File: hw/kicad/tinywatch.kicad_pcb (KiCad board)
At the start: 2 copper layers, 24.9 x 23.1 mm, 18 parts, among them J1 Conn_01x04, J2 Conn_01x30, SW1 SW_Push, SW2 SW_Push, SW3 SW_Push, U1 ATtiny1614-SS

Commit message: R2 hardware
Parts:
- removed R1: 4k7, Resistor_SMD:R_0603_1608Metric_Pad0.98x0.95mm_HandSolder
- added C10: 8.2p, Capacitor_SMD:C_0603_1608Metric_Pad1.08x0.95mm_HandSolder, F.Cu at (166.9, 87.5)
- added C9: 8.2p, Capacitor_SMD:C_0603_1608Metric_Pad1.08x0.95mm_HandSolder, F.Cu at (166.9, 84.2)
- added J3: Conn_01x01_Pin, Connector_Wire:SolderWire-0.25sqmm_1x01_D0.65mm_OD1.7mm, F.Cu at (148.2, 99.9)
- added J4: Conn_01x01_Pin, Connector_Wire:SolderWire-0.25sqmm_1x01_D0.65mm_OD1.7mm, F.Cu at (159.5, 99.9)
- added Y1: 32.768 kHz, Crystal:Crystal_DS10_D1.0mm_L4.3mm_Horizontal, F.Cu at (164.1, 88.8)
- moved U1 4.56 mm to (161.5, 82.3)
- moved C2 3.84 mm to (165.9, 87.4)
- moved C3 3.84 mm to (162.1, 87.4)
- moved C5 3.13 mm to (155.3, 84.8)
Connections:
- J1 pad 1: Net-(J1-Pad1) -> Net-(J1-Pin_1)
- J1 pad 2: Net-(J1-Pad2) -> Net-(J1-Pin_2)
- J1 pad 3: Net-(J1-Pad3) -> Net-(J1-Pin_3)
- U1 pad 10: Net-(R1-Pad2) -> Net-(J1-Pin_3)
- U1 pad 11: VCCQ -> Net-(J1-Pin_2)
- U1 pad 12: unconnected-(U1-Pad12) -> Net-(J1-Pin_1)
- U1 pad 2: unconnected-(U1-Pad2) -> VCCQ
- U1 pad 6: Net-(J1-Pad1) -> Net-(U1-PB3)
- U1 pad 7: Net-(J1-Pad2) -> Net-(U1-PB2)
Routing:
- net GND: track 65.0 -> 0.00 mm, vias 1 -> 2
- net Net-(J1-Pad1): track 31.3 -> 0.00 mm
- net Net-(J1-Pad2): track 24.8 -> 0.00 mm
- net Net-(J1-Pin_3): track 0.00 -> 14.4 mm
- net Net-(J1-Pin_2): track 0.00 -> 12.3 mm
- net Net-(J1-Pin_1): track 0.00 -> 10.8 mm
- net VCC: track 29.2 -> 20.0 mm
- net Net-(R1-Pad2): track 9.00 -> 0.00 mm
- net Net-(U1-PB3): track 0.00 -> 7.94 mm
- net Net-(U1-PB2): track 0.00 -> 7.78 mm
- net Net-(U1-PA7): track 6.33 -> 12.2 mm
- net Net-(J2-Pin_18): track 14.2 -> 19.3 mm
- net Net-(U1-PA6): track 5.20 -> 10.0 mm
- net Net-(U1-PA5): track 13.1 -> 17.2 mm
- net Net-(J2-Pin_3): track 6.74 -> 3.38 mm
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
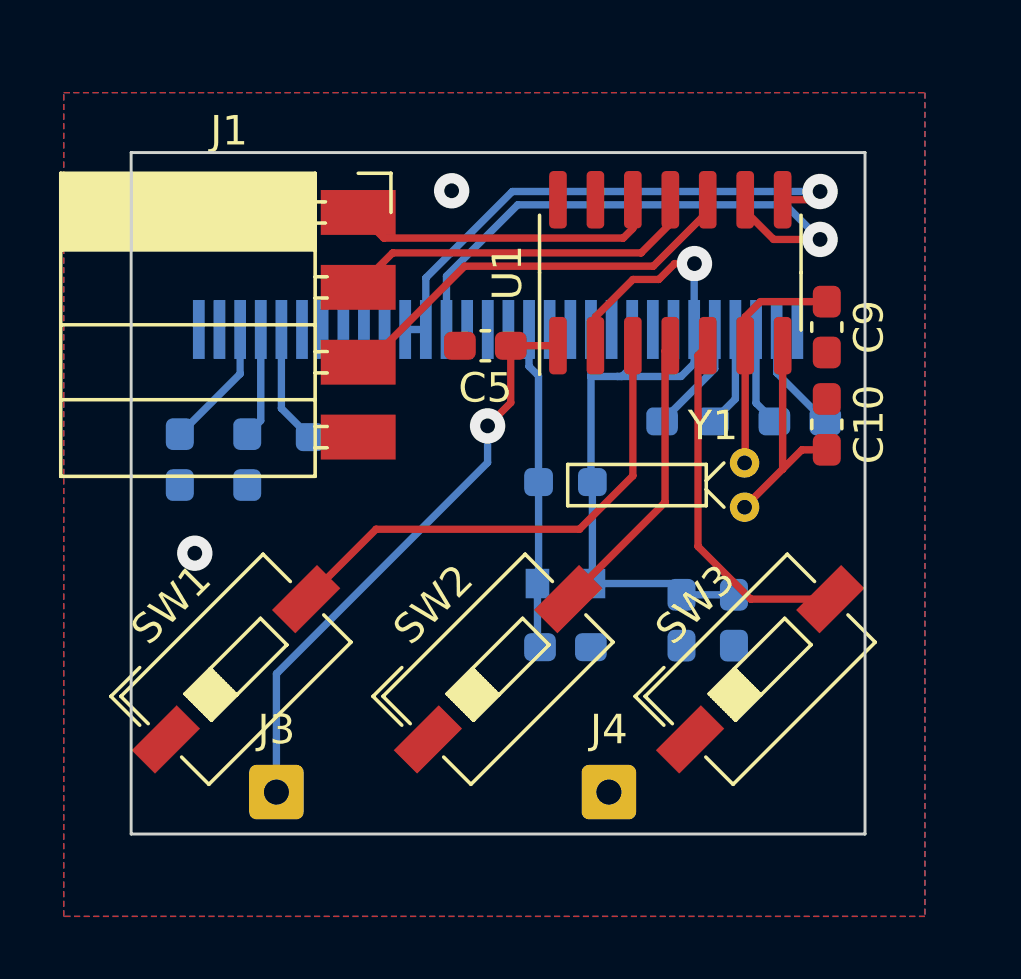
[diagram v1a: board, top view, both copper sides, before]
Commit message: Updated BOM and README
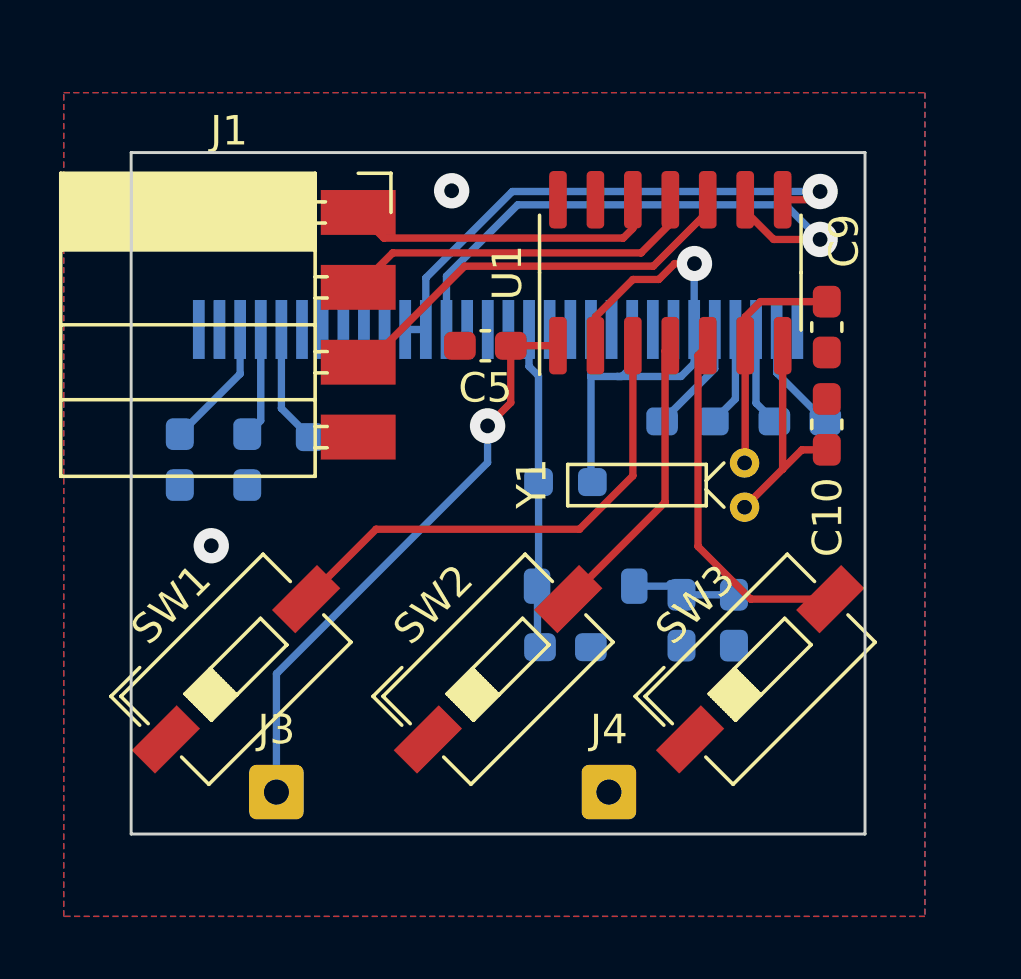
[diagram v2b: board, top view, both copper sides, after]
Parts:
- D1: footprint Diode_SMD:D_SOD-110 -> Diode_SMD:D_SOD-123
- moved D1 0.69 mm to (158.7, 92.9)
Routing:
- net VCCQ: track 27.6 -> 23.3 mm

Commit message: Left a trace disconnected, whoops
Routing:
- net VCCQ: track 23.3 -> 27.4 mm

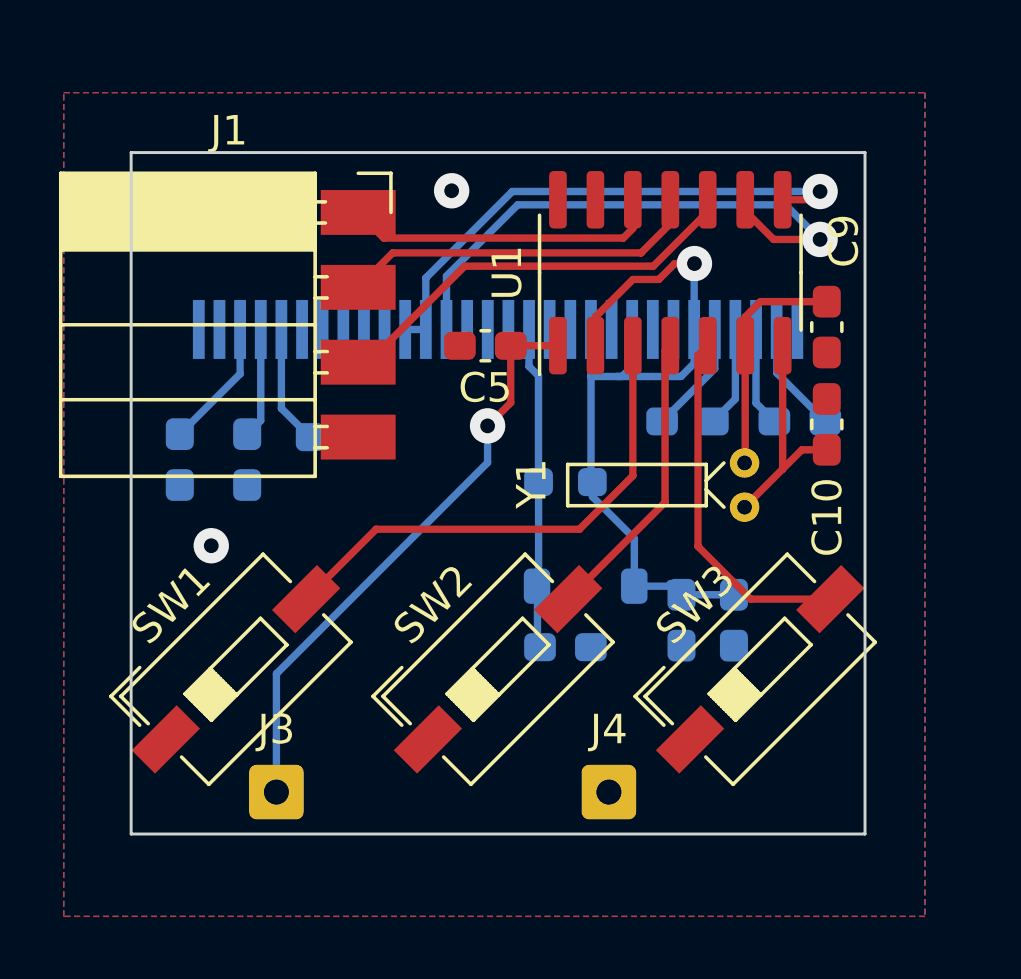
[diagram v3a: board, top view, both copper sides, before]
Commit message: Replaced the crystal with a more precise TXCO
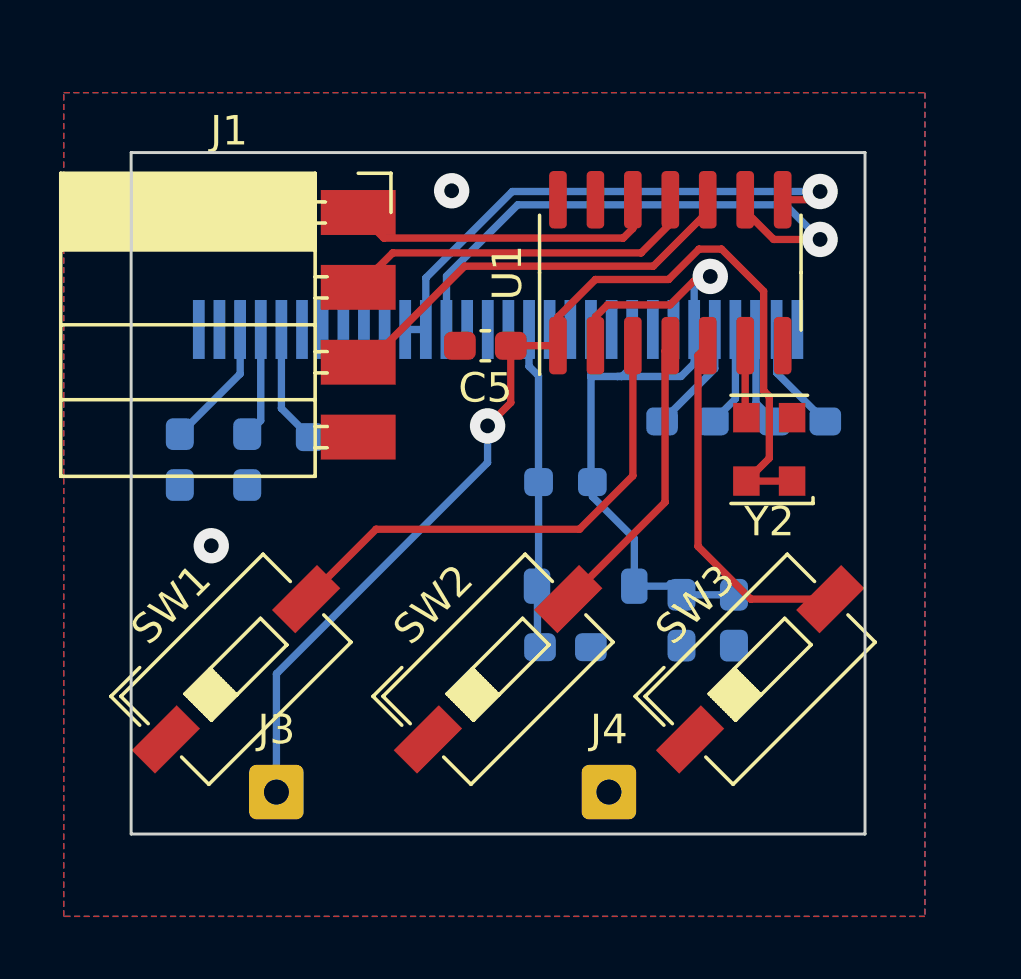
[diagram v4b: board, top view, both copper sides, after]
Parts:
- removed C10, C9: 8.2p, Capacitor_SMD:C_0603_1608Metric_Pad1.08x0.95mm_HandSolder
- removed Y1: 32.768 kHz, Crystal:Crystal_DS10_D1.0mm_L4.3mm_Horizontal
- added Y2: ECS-327TXO-30, Oscillator:Oscillator_SMD_EuroQuartz_XO32-4Pin_3.2x2.5mm, F.Cu at (164.9, 88.3)
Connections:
- U1 pad 7: Net-(U1-PB2) -> unconnected-(U1-PB2-Pad7)
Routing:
- net VCC: track 20.0 -> 37.9 mm
- net Net-(U1-PB2): track 7.78 -> 0.00 mm
- net Net-(U1-PB3): track 7.94 -> 2.46 mm

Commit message: Replaced TXCO footprint with a more solderable variant
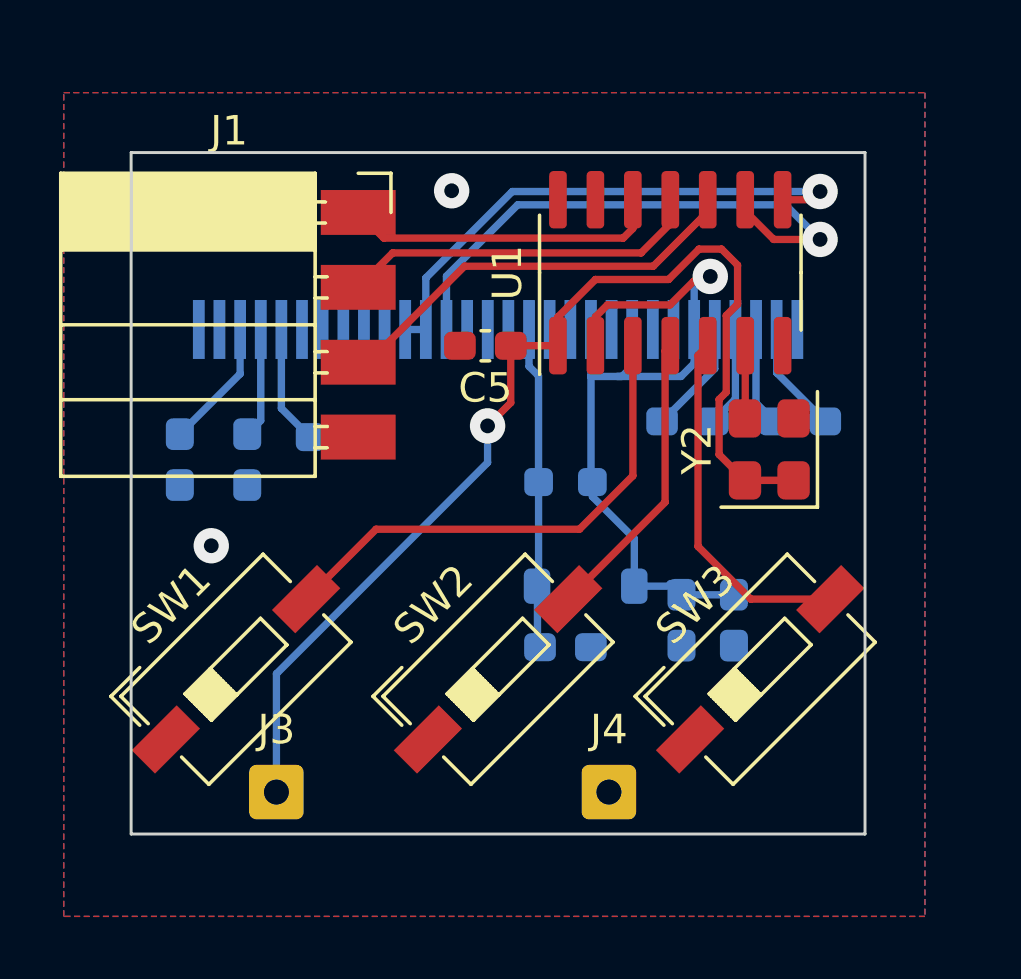
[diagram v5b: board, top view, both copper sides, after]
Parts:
- Y2: footprint Oscillator:Oscillator_SMD_EuroQuartz_XO32-4Pin_3.2x2.5mm -> Oscillator:Oscillator_SMD_Abracon_ASE-4Pin_3.2x2.5mm
- turned Y2 to 90 degrees

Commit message: Added labels for "+" and "-"
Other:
- board text added: "+"
- board text added: "-"
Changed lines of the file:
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@@
 		(layer "Edge.Cuts")
+	)
+	(gr_text "+"
+		(at 149.7836 99.9236 0)
+		(layer "B.SilkS")
+		(effects
+			(font
+				(size 1 1)
+				(thickness 0.15)
+			)
+			(justify right mirror)
+		)
+	)
+	(gr_text "-"
+		(at 161.0612 99.9236 0)
+		(layer "B.SilkS")
+		(effects
+			(font
+				(size 1 1)
+				(thickness 0.15)
+			)
+			(justify right mirror)
+		)
 	)
 	(segment

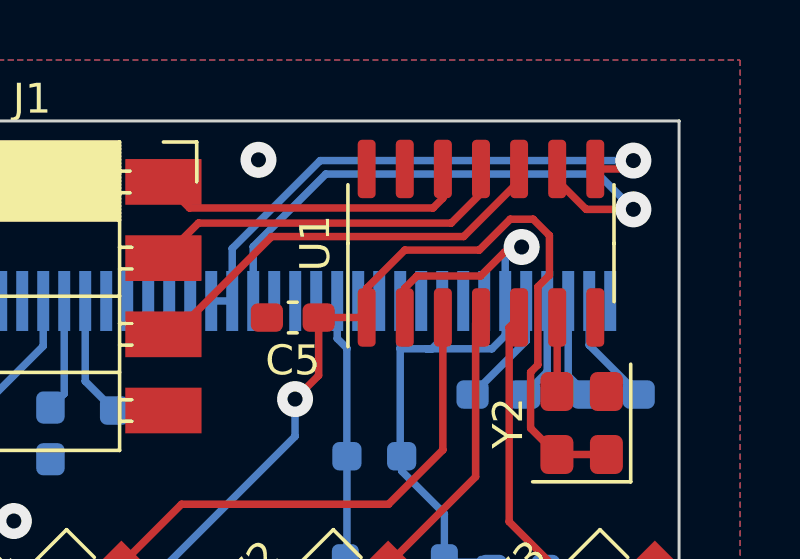
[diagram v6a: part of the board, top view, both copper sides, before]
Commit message: Updated to ATtiny3224
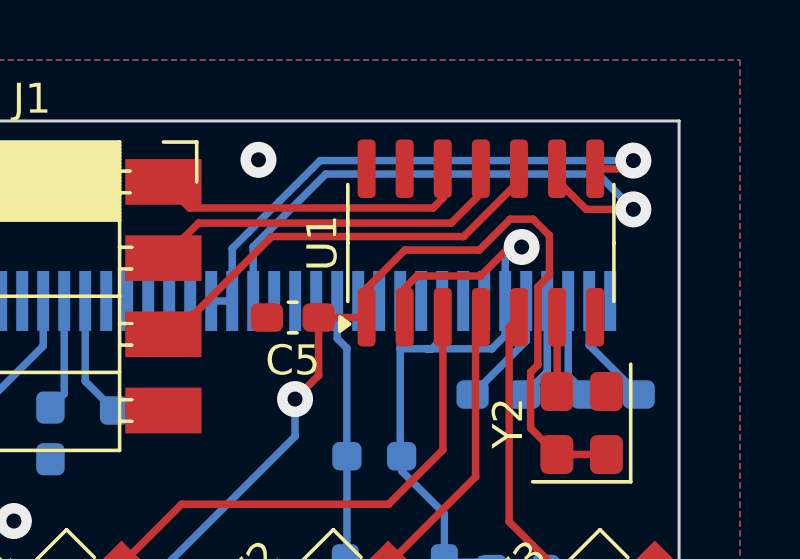
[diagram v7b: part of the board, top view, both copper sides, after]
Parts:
- U1: value ATtiny1614-SS -> ATtiny3224-SS
